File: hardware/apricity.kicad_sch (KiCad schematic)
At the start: 26 parts, among them J1 USB_C_Receptacle_USB2.0, U1 ESP-WROOM-02D, U2 X

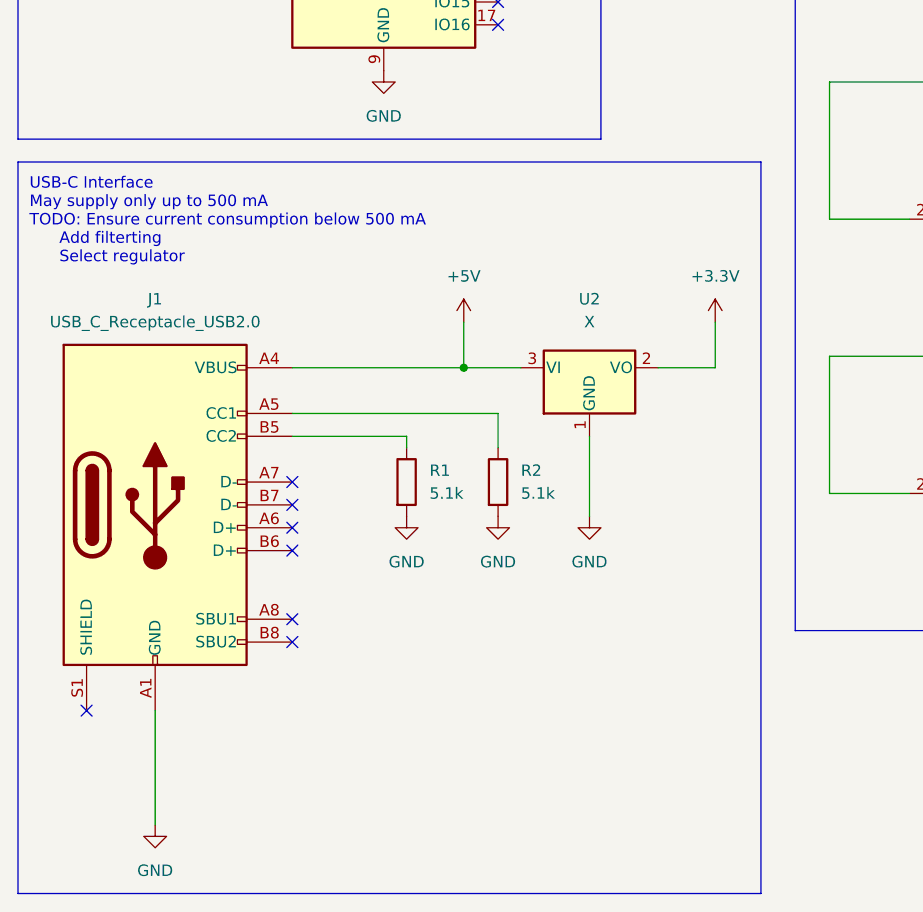
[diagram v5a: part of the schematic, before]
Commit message: remove led vias from pads
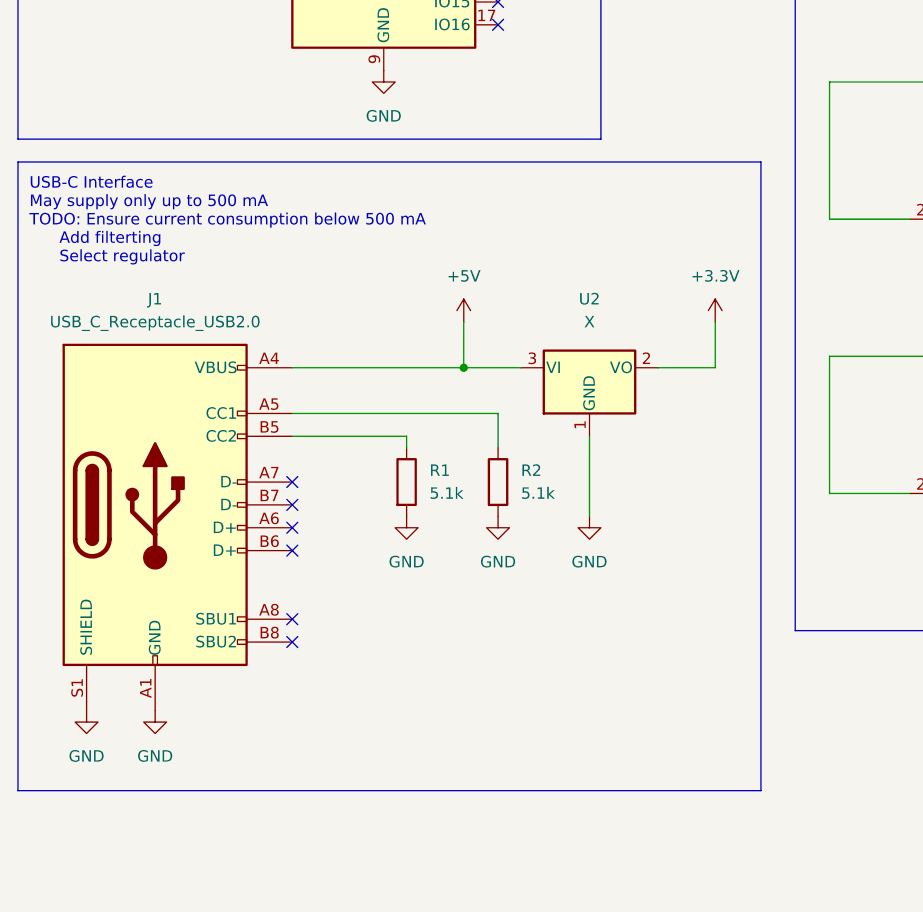
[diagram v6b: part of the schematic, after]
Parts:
- J1: footprint Connector_USB:USB_C_Receptacle_XKB_U262-16XN-4BVC11 -> Connector_USB:USB_C_Receptacle_Palconn_UTC16-G
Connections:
- net GND: now also J1.S1 (SHIELD)
- no-connect marks 20 -> 19
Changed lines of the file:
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@@
   )
   (no_connect (at 45.72 143.51))
-  (no_connect (at 22.86 153.67))
   (no_connect (at 68.58 77.47))
   (no_connect (at 68.58 64.77))
@@
     (stroke (width 0) (type default) (color 0 0 0 0))
   )
-  (wire (pts (xy 30.48 153.67) (xy 30.48 166.37))
-    (stroke (width 0) (type default) (color 0 0 0 0))
-  )
   (wire (pts (xy 68.58 67.31) (xy 73.66 67.31))
     (stroke (width 0) (type default) (color 0 0 0 0))
@@
     (stroke (width 0) (type default) (color 0 0 0 0))
   )
+  (polyline (pts (xy 15.24 162.56) (xy 97.79 162.56))
+    (stroke (width 0) (type default) (color 0 0 0 0))
+  )
   (wire (pts (xy 271.78 68.58) (xy 262.89 68.58))
     (stroke (width 0) (type default) (color 0 0 0 0))
@@
     (stroke (width 0) (type default) (color 0 0 0 0))
   )
-  (polyline (pts (xy 15.24 92.71) (xy 15.24 173.99))
+  (polyline (pts (xy 15.24 92.71) (xy 15.24 162.56))
     (stroke (width 0) (type default) (color 0 0 0 0))
   )
@@
     (stroke (width 0) (type default) (color 0 0 0 0))
   )
-  (polyline (pts (xy 15.24 173.99) (xy 97.79 173.99))
-    (stroke (width 0) (type default) (color 0 0 0 0))
-  )
   (wire (pts (xy 45.72 115.57) (xy 64.77 115.57))
     (stroke (width 0) (type default) (color 0 0 0 0))
   )
-  (polyline (pts (xy 97.79 173.99) (xy 97.79 92.71))
+  (polyline (pts (xy 97.79 162.56) (xy 97.79 92.71))
     (stroke (width 0) (type default) (color 0 0 0 0))
   )
@@
     (pin "2")
   )
+  (symbol (lib_id "power:GND") (at 22.86 153.67 0) (unit 1)
+    (in_bom yes) (on_board yes) (fields_autoplaced)
+    (property "Reference" "#PWR0101" (id 0) (at 22.86 160.02 0)
+      (effects (font (size 1.27 1.27)) hide)
+    )
+    (property "Value" "GND" (id 1) (at 22.86 158.75 0))
+    (property "Footprint" "" (id 2) (at 22.86 153.67 0)
+      (effects (font (size 1.27 1.27)) hide)
+    )
+    (property "Datasheet" "" (id 3) (at 22.86 153.67 0)
+      (effects (font (size 1.27 1.27)) hide)
+    )
+    (pin "1")
+  )
   (symbol (lib_id "LED:Inolux_IN-PI554FCH") (at 156.21 68.58 0) (unit 1)
     (in_bom yes) (on_board yes) (fields_autoplaced)
@@
     (pin "1")
   )
-  (symbol (lib_id "power:GND") (at 30.48 166.37 0) (unit 1)
-    (in_bom yes) (on_board yes) (fields_autoplaced)
-    (property "Reference" "#PWR050" (id 0) (at 30.48 172.72 0)
-      (effects (font (size 1.27 1.27)) hide)
-    )
-    (property "Value" "GND" (id 1) (at 30.48 171.45 0))
-    (property "Footprint" "" (id 2) (at 30.48 166.37 0)
-      (effects (font (size 1.27 1.27)) hide)
-    )
-    (property "Datasheet" "" (id 3) (at 30.48 166.37 0)
+  (symbol (lib_id "power:GND") (at 30.48 153.67 0) (unit 1)
+    (in_bom yes) (on_board yes) (fields_autoplaced)
+    (property "Reference" "#PWR050" (id 0) (at 30.48 160.02 0)
+      (effects (font (size 1.27 1.27)) hide)
+    )
+    (property "Value" "GND" (id 1) (at 30.48 158.75 0))
+    (property "Footprint" "" (id 2) (at 30.48 153.67 0)
+      (effects (font (size 1.27 1.27)) hide)
+    )
+    (property "Datasheet" "" (id 3) (at 30.48 153.67 0)
       (effects (font (size 1.27 1.27)) hide)
     )
@@
     (property "Reference" "J1" (id 0) (at 30.48 107.95 0))
     (property "Value" "USB_C_Receptacle_USB2.0" (id 1) (at 30.48 110.49 0))
-    (property "Footprint" "Connector_USB:USB_C_Receptacle_XKB_U262-16XN-4BVC11" (id 2) (at 34.29 130.81 0)
+    (property "Footprint" "Connector_USB:USB_C_Receptacle_Palconn_UTC16-G" (id 2) (at 34.29 130.81 0)
       (effects (font (size 1.27 1.27)) hide)
     )
@@
       (reference "#PWR050") (unit 1) (value "GND") (footprint "")
     )
+    (path "/9eb07467-e9a3-42e2-ad66-766dccaed89b"
+      (reference "#PWR0101") (unit 1) (value "GND") (footprint "")
+    )
     (path "/72000050-10f4-4e4a-8408-f3012295f71a"
       (reference "C1") (unit 1) (value "0.1u") (footprint "Capacitor_SMD:C_1206_3216Metric")
@@
     )
     (path "/efec80d5-3b93-449b-967c-e6308c2f145f"
-      (reference "J1") (unit 1) (value "USB_C_Receptacle_USB2.0") (footprint "Connector_USB:USB_C_Receptacle_XKB_U262-16XN-4BVC11")
+      (reference "J1") (unit 1) (value "USB_C_Receptacle_USB2.0") (footprint "Connector_USB:USB_C_Receptacle_Palconn_UTC16-G")
     )
     (path "/0d05b2dd-0847-494b-a812-c82d7fd47262"

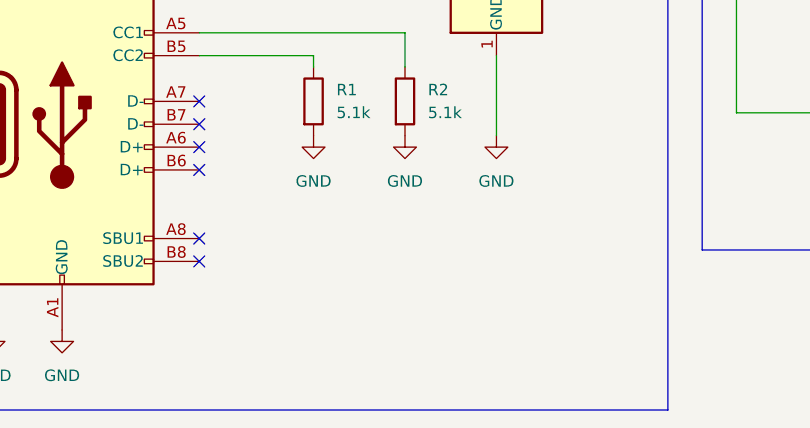
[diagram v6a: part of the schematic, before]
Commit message: use jumper to connect power trace
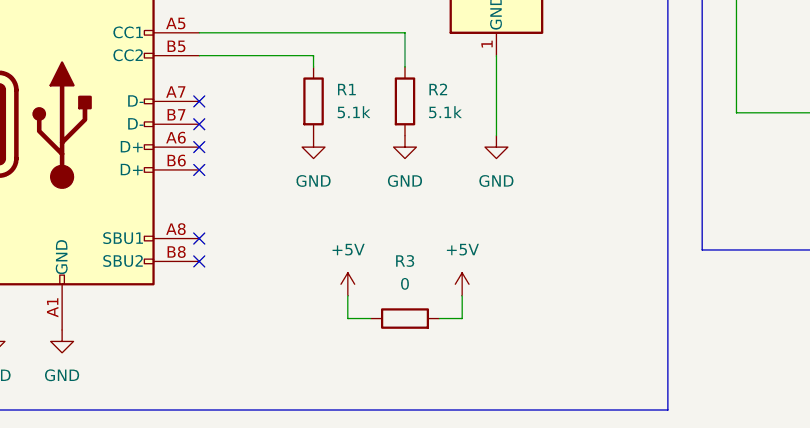
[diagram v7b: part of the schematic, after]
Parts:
- added R3: 0, Resistor_SMD:R_0805_2012Metric_Pad1.20x1.40mm_HandSolder, symbol Device:R
- R1, R2: footprint Resistor_SMD:R_0805_2012Metric -> Resistor_SMD:R_0805_2012Metric_Pad1.20x1.40mm_HandSolder
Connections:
- net +5V: now also R3.1, R3.2
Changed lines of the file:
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@@
+    (stroke (width 0) (type default) (color 0 0 0 0))
+  )
+  (wire (pts (xy 62.23 149.86) (xy 62.23 152.4))
     (stroke (width 0) (type default) (color 0 0 0 0))
   )
@@
     (stroke (width 0) (type default) (color 0 0 0 0))
   )
+  (wire (pts (xy 62.23 152.4) (xy 64.77 152.4))
+    (stroke (width 0) (type default) (color 0 0 0 0))
+  )
   (wire (pts (xy 78.74 123.19) (xy 78.74 132.08))
     (stroke (width 0) (type default) (color 0 0 0 0))
@@
     (stroke (width 0) (type default) (color 0 0 0 0))
   )
+  (wire (pts (xy 74.93 152.4) (xy 72.39 152.4))
+    (stroke (width 0) (type default) (color 0 0 0 0))
+  )
   (wire (pts (xy 229.87 99.06) (xy 247.65 99.06))
     (stroke (width 0) (type default) (color 0 0 0 0))
@@
   )
   (polyline (pts (xy 15.24 162.56) (xy 97.79 162.56))
+    (stroke (width 0) (type default) (color 0 0 0 0))
+  )
+  (wire (pts (xy 74.93 149.86) (xy 74.93 152.4))
     (stroke (width 0) (type default) (color 0 0 0 0))
   )
@@
     (pin "1")
   )
+  (symbol (lib_id "power:+5V") (at 62.23 149.86 0) (unit 1)
+    (in_bom yes) (on_board yes) (fields_autoplaced)
+    (property "Reference" "#PWR049" (id 0) (at 62.23 153.67 0)
+      (effects (font (size 1.27 1.27)) hide)
+    )
+    (property "Value" "+5V" (id 1) (at 62.23 144.78 0))
+    (property "Footprint" "" (id 2) (at 62.23 149.86 0)
+      (effects (font (size 1.27 1.27)) hide)
+    )
+    (property "Datasheet" "" (id 3) (at 62.23 149.86 0)
+      (effects (font (size 1.27 1.27)) hide)
+    )
+    (pin "1")
+  )
   (symbol (lib_id "power:+5V") (at 189.23 91.44 0) (unit 1)
     (in_bom yes) (on_board yes) (fields_autoplaced)
@@
       (effects (font (size 1.27 1.27)) (justify left))
     )
-    (property "Footprint" "Resistor_SMD:R_0805_2012Metric" (id 2) (at 56.642 128.27 90)
+    (property "Footprint" "Resistor_SMD:R_0805_2012Metric_Pad1.20x1.40mm_HandSolder" (id 2) (at 56.642 128.27 90)
       (effects (font (size 1.27 1.27)) hide)
     )
@@
     (pin "4")
   )
+  (symbol (lib_id "power:+5V") (at 74.93 149.86 0) (unit 1)
+    (in_bom yes) (on_board yes) (fields_autoplaced)
+    (property "Reference" "#PWR050" (id 0) (at 74.93 153.67 0)
+      (effects (font (size 1.27 1.27)) hide)
+    )
+    (property "Value" "+5V" (id 1) (at 74.93 144.78 0))
+    (property "Footprint" "" (id 2) (at 74.93 149.86 0)
+      (effects (font (size 1.27 1.27)) hide)
+    )
+    (property "Datasheet" "" (id 3) (at 74.93 149.86 0)
+      (effects (font (size 1.27 1.27)) hide)
+    )
+    (pin "1")
+  )
   (symbol (lib_id "power:+5V") (at 121.92 29.21 0) (unit 1)
     (in_bom yes) (on_board yes) (fields_autoplaced)
@@
       (effects (font (size 1.27 1.27)) (justify left))
     )
-    (property "Footprint" "Resistor_SMD:R_0805_2012Metric" (id 2) (at 66.802 128.27 90)
+    (property "Footprint" "Resistor_SMD:R_0805_2012Metric_Pad1.20x1.40mm_HandSolder" (id 2) (at 66.802 128.27 90)
       (effects (font (size 1.27 1.27)) hide)
     )
@@
   (symbol (lib_id "power:GND") (at 22.86 153.67 0) (unit 1)
     (in_bom yes) (on_board yes) (fields_autoplaced)
-    (property "Reference" "#PWR0101" (id 0) (at 22.86 160.02 0)
+    (property "Reference" "#PWR051" (id 0) (at 22.86 160.02 0)
       (effects (font (size 1.27 1.27)) hide)
     )
@@
     (pin "4")
   )
+  (symbol (lib_id "Device:R") (at 68.58 152.4 90) (unit 1)
+    (in_bom yes) (on_board yes) (fields_autoplaced)
+    (property "Reference" "R3" (id 0) (at 68.58 146.05 90))
+    (property "Value" "0" (id 1) (at 68.58 148.59 90))
+    (property "Footprint" "Resistor_SMD:R_0805_2012Metric_Pad1.20x1.40mm_HandSolder" (id 2) (at 68.58 154.178 90)
+      (effects (font (size 1.27 1.27)) hide)
+    )
+    (property "Datasheet" "~" (id 3) (at 68.58 152.4 0)
+      (effects (font (size 1.27 1.27)) hide)
+    )
+    (pin "1")
+    (pin "2")
+  )
   (symbol (lib_id "power:+5V") (at 121.92 60.96 0) (unit 1)
     (in_bom yes) (on_board yes) (fields_autoplaced)
@@
   (symbol (lib_id "power:GND") (at 30.48 153.67 0) (unit 1)
     (in_bom yes) (on_board yes) (fields_autoplaced)
-    (property "Reference" "#PWR050" (id 0) (at 30.48 160.02 0)
+    (property "Reference" "#PWR052" (id 0) (at 30.48 160.02 0)
       (effects (font (size 1.27 1.27)) hide)
     )
@@
       (reference "#PWR048") (unit 1) (value "GND") (footprint "")
     )
+    (path "/07f960a3-41d8-48f1-8302-2fbb24405fed"
+      (reference "#PWR049") (unit 1) (value "+5V") (footprint "")
+    )
+    (path "/584bd144-f0b6-4cf3-8d9d-add5182a1e97"
+      (reference "#PWR050") (unit 1) (value "+5V") (footprint "")
+    )
+    (path "/9eb07467-e9a3-42e2-ad66-766dccaed89b"
+      (reference "#PWR051") (unit 1) (value "GND") (footprint "")
+    )
     (path "/e2c4a6fe-1e37-465a-8920-4c4fc7446705"
-      (reference "#PWR050") (unit 1) (value "GND") (footprint "")
-    )
-    (path "/9eb07467-e9a3-42e2-ad66-766dccaed89b"
-      (reference "#PWR0101") (unit 1) (value "GND") (footprint "")
+      (reference "#PWR052") (unit 1) (value "GND") (footprint "")
     )
     (path "/72000050-10f4-4e4a-8408-f3012295f71a"
@@
     )
     (path "/0d05b2dd-0847-494b-a812-c82d7fd47262"
-      (reference "R1") (unit 1) (value "5.1k") (footprint "Resistor_SMD:R_0805_2012Metric")
+      (reference "R1") (unit 1) (value "5.1k") (footprint "Resistor_SMD:R_0805_2012Metric_Pad1.20x1.40mm_HandSolder")
     )
     (path "/9ccddcfc-2737-450b-ad5a-9c18babfb3bf"
-      (reference "R2") (unit 1) (value "5.1k") (footprint "Resistor_SMD:R_0805_2012Metric")
+      (reference "R2") (unit 1) (value "5.1k") (footprint "Resistor_SMD:R_0805_2012Metric_Pad1.20x1.40mm_HandSolder")
+    )
+    (path "/d0c6389e-4f26-40a2-b6ef-fbdb07438c13"
+      (reference "R3") (unit 1) (value "0") (footprint "Resistor_SMD:R_0805_2012Metric_Pad1.20x1.40mm_HandSolder")
     )
     (path "/0db9c4c6-e8b9-4e75-813c-bf63da48c2f4"

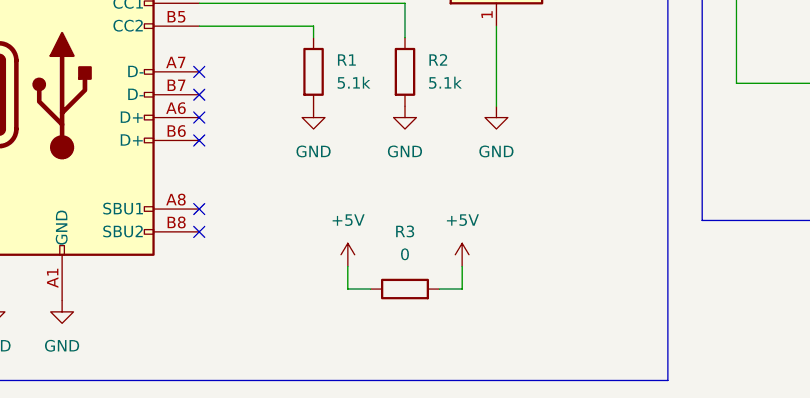
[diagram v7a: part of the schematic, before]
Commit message: fix routing issues with jumper
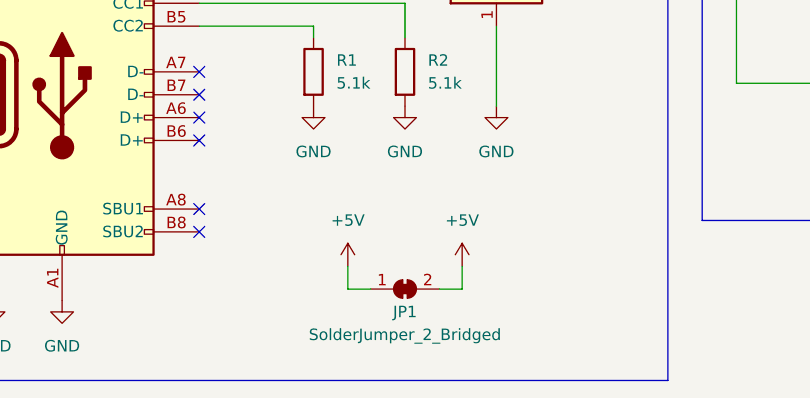
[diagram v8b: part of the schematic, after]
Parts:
- removed R3: 0, Resistor_SMD:R_0805_2012Metric_Pad1.20x1.40mm_HandSolder, symbol Device:R
- added JP1: SolderJumper_2_Bridged, Resistor_SMD:R_0805_2012Metric_Pad1.20x1.40mm_HandSolder, symbol Jumper:SolderJumper_2_Bridged
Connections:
- net +5V: now also JP1.1 (A), JP1.2 (B)
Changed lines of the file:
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@@
     (pin "1")
+  )
+  (symbol (lib_id "Jumper:SolderJumper_2_Bridged") (at 68.58 152.4 0) (unit 1)
+    (in_bom yes) (on_board yes)
+    (property "Reference" "JP1" (id 0) (at 68.58 154.94 0))
+    (property "Value" "SolderJumper_2_Bridged" (id 1) (at 68.58 157.48 0))
+    (property "Footprint" "Resistor_SMD:R_0805_2012Metric_Pad1.20x1.40mm_HandSolder" (id 2) (at 68.58 152.4 0)
+      (effects (font (size 1.27 1.27)) hide)
+    )
+    (property "Datasheet" "~" (id 3) (at 68.58 152.4 0)
+      (effects (font (size 1.27 1.27)) hide)
+    )
+    (pin "1")
+    (pin "2")
   )
   (symbol (lib_id "LED:Inolux_IN-PI554FCH") (at 189.23 99.06 0) (unit 1)
@@
     (pin "4")
   )
-  (symbol (lib_id "power:+5V") (at 74.93 149.86 0) (unit 1)
-    (in_bom yes) (on_board yes) (fields_autoplaced)
-    (property "Reference" "#PWR050" (id 0) (at 74.93 153.67 0)
-      (effects (font (size 1.27 1.27)) hide)
-    )
-    (property "Value" "+5V" (id 1) (at 74.93 144.78 0))
-    (property "Footprint" "" (id 2) (at 74.93 149.86 0)
-      (effects (font (size 1.27 1.27)) hide)
-    )
-    (property "Datasheet" "" (id 3) (at 74.93 149.86 0)
-      (effects (font (size 1.27 1.27)) hide)
-    )
-    (pin "1")
-  )
   (symbol (lib_id "power:+5V") (at 121.92 29.21 0) (unit 1)
     (in_bom yes) (on_board yes) (fields_autoplaced)
@@
   (symbol (lib_id "power:GND") (at 22.86 153.67 0) (unit 1)
     (in_bom yes) (on_board yes) (fields_autoplaced)
-    (property "Reference" "#PWR051" (id 0) (at 22.86 160.02 0)
+    (property "Reference" "#PWR050" (id 0) (at 22.86 160.02 0)
       (effects (font (size 1.27 1.27)) hide)
     )
@@
     (pin "4")
   )
-  (symbol (lib_id "Device:R") (at 68.58 152.4 90) (unit 1)
-    (in_bom yes) (on_board yes) (fields_autoplaced)
-    (property "Reference" "R3" (id 0) (at 68.58 146.05 90))
-    (property "Value" "0" (id 1) (at 68.58 148.59 90))
-    (property "Footprint" "Resistor_SMD:R_0805_2012Metric_Pad1.20x1.40mm_HandSolder" (id 2) (at 68.58 154.178 90)
-      (effects (font (size 1.27 1.27)) hide)
-    )
-    (property "Datasheet" "~" (id 3) (at 68.58 152.4 0)
-      (effects (font (size 1.27 1.27)) hide)
-    )
-    (pin "1")
-    (pin "2")
-  )
   (symbol (lib_id "power:+5V") (at 121.92 60.96 0) (unit 1)
     (in_bom yes) (on_board yes) (fields_autoplaced)
@@
     (pin "4")
   )
+  (symbol (lib_name "+5V_1") (lib_id "power:+5V") (at 74.93 149.86 0) (unit 1)
+    (in_bom yes) (on_board yes) (fields_autoplaced)
+    (property "Reference" "#PWR?" (id 0) (at 74.93 153.67 0)
+      (effects (font (size 1.27 1.27)) hide)
+    )
+    (property "Value" "+5V" (id 1) (at 74.93 144.78 0))
+    (property "Footprint" "" (id 2) (at 74.93 149.86 0)
+      (effects (font (size 1.27 1.27)) hide)
+    )
+    (property "Datasheet" "" (id 3) (at 74.93 149.86 0)
+      (effects (font (size 1.27 1.27)) hide)
+    )
+    (pin "1")
+  )
   (symbol (lib_id "power:GND") (at 189.23 44.45 0) (unit 1)
     (in_bom yes) (on_board yes) (fields_autoplaced)
@@
   (symbol (lib_id "power:GND") (at 30.48 153.67 0) (unit 1)
     (in_bom yes) (on_board yes) (fields_autoplaced)
-    (property "Reference" "#PWR052" (id 0) (at 30.48 160.02 0)
+    (property "Reference" "#PWR051" (id 0) (at 30.48 160.02 0)
       (effects (font (size 1.27 1.27)) hide)
     )
@@
       (reference "#PWR049") (unit 1) (value "+5V") (footprint "")
     )
-    (path "/584bd144-f0b6-4cf3-8d9d-add5182a1e97"
-      (reference "#PWR050") (unit 1) (value "+5V") (footprint "")
-    )
     (path "/9eb07467-e9a3-42e2-ad66-766dccaed89b"
+      (reference "#PWR050") (unit 1) (value "GND") (footprint "")
+    )
+    (path "/e2c4a6fe-1e37-465a-8920-4c4fc7446705"
       (reference "#PWR051") (unit 1) (value "GND") (footprint "")
     )
-    (path "/e2c4a6fe-1e37-465a-8920-4c4fc7446705"
-      (reference "#PWR052") (unit 1) (value "GND") (footprint "")
+    (path "/da82756c-23f4-4c94-932b-8de9e93f4c87"
+      (reference "#PWR?") (unit 1) (value "+5V") (footprint "")
     )
     (path "/72000050-10f4-4e4a-8408-f3012295f71a"
@@
       (reference "J1") (unit 1) (value "USB_C_Receptacle_USB2.0") (footprint "Connector_USB:USB_C_Receptacle_Palconn_UTC16-G")
     )
+    (path "/1f89d10a-d9d3-44c4-8a94-f8943d474c0e"
+      (reference "JP1") (unit 1) (value "SolderJumper_2_Bridged") (footprint "Resistor_SMD:R_0805_2012Metric_Pad1.20x1.40mm_HandSolder")
+    )
     (path "/0d05b2dd-0847-494b-a812-c82d7fd47262"
       (reference "R1") (unit 1) (value "5.1k") (footprint "Resistor_SMD:R_0805_2012Metric_Pad1.20x1.40mm_HandSolder")
@@
       (reference "R2") (unit 1) (value "5.1k") (footprint "Resistor_SMD:R_0805_2012Metric_Pad1.20x1.40mm_HandSolder")
     )
-    (path "/d0c6389e-4f26-40a2-b6ef-fbdb07438c13"
-      (reference "R3") (unit 1) (value "0") (footprint "Resistor_SMD:R_0805_2012Metric_Pad1.20x1.40mm_HandSolder")
-    )
     (path "/0db9c4c6-e8b9-4e75-813c-bf63da48c2f4"
